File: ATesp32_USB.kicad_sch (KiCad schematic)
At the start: 17 parts, among them J1 USB_C_Receptacle_USB2.0_16P, U5 CP2102N-Axx-xQFN24

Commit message: update manf outputs
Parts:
- C15: Mouser 187-CL05B104KO5NNNC -> (none)
- U5: DigiKey (none) -> 336-5887-ND
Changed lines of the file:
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@@
 			)
 		)
-		(property "Mouser" "187-CL05B104KO5NNNC"
+		(property "Mouser" ""
 			(at 60.96 38.1 0)
 			(effects
@@
 			(at 85.09 73.66 0)
 			(effects
+				(font
+					(size 1.27 1.27)
+				)
+				(hide yes)
+			)
+		)
+		(property "DigiKey" "336-5887-ND"
+			(at 85.09 73.66 0)
+			(effects

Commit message: USB-UART Bridge LEDs had wrong orientation. Fixed
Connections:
- net GND: now also D5.1 (K), D6.1 (K); no longer D5.2 (A), D6.2 (A)
- net at R15.2: now also D6.2 (A); no longer D6.1 (K)
- net at R14.2: now also D5.2 (A); no longer D5.1 (K)
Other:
- moved on the sheet: D5, D6
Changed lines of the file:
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@@
 	(symbol
 		(lib_id "Device:LED_Small")
-		(at 105.41 92.71 270)
+		(at 105.41 92.71 90)
 		(unit 1)
 		(exclude_from_sim no)
@@
 		(fields_autoplaced yes)
 		(property "Reference" "D6"
-			(at 107.95 91.5034 90)
-			(effects
-				(font
-					(size 1.27 1.27)
-				)
-				(justify left)
+			(at 107.95 91.3764 90)
+			(effects
+				(font
+					(size 1.27 1.27)
+				)
+				(justify right)
 			)
 		)
 		(property "Value" "LED_Small"
-			(at 107.95 94.0434 90)
-			(effects
-				(font
-					(size 1.27 1.27)
-				)
-				(justify left)
+			(at 107.95 93.9164 90)
+			(effects
+				(font
+					(size 1.27 1.27)
+				)
+				(justify right)
 			)
 		)
@@
 	(symbol
 		(lib_id "Device:LED_Small")
-		(at 119.38 97.79 270)
+		(at 119.38 97.79 90)
 		(unit 1)
 		(exclude_from_sim no)
@@
 		(fields_autoplaced yes)
 		(property "Reference" "D5"
-			(at 121.92 96.5834 90)
-			(effects
-				(font
-					(size 1.27 1.27)
-				)
-				(justify left)
+			(at 121.92 96.4564 90)
+			(effects
+				(font
+					(size 1.27 1.27)
+				)
+				(justify right)
 			)
 		)
 		(property "Value" "LED_Small"
-			(at 121.92 99.1234 90)
-			(effects
-				(font
-					(size 1.27 1.27)
-				)
-				(justify left)
-			)
-		)
+			(at 121.92 98.9964 90)
+			(effects
+				(font
+					(size 1.27 1.27)
+				)
+				(justify right)
+			)
+		)

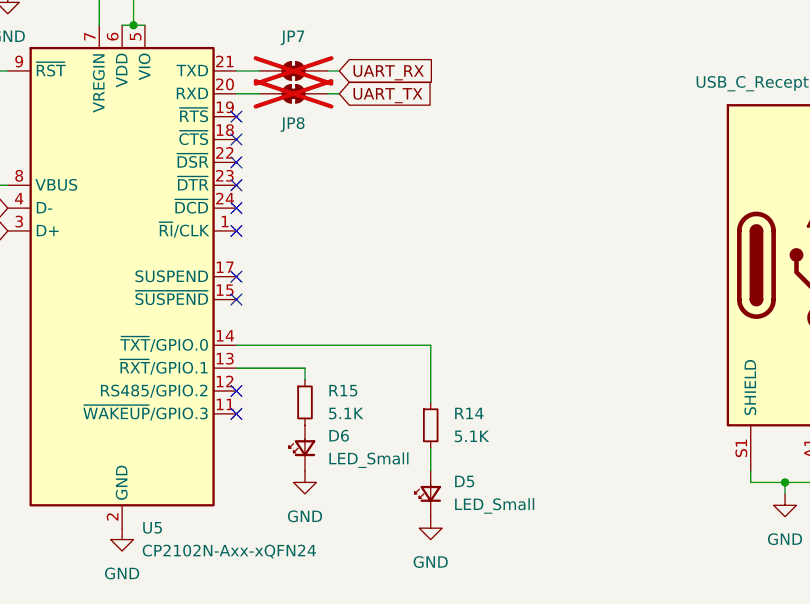
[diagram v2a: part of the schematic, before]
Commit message: LEDs were persistently on. Change to active low config see CP2102N datasheet fig 4.3
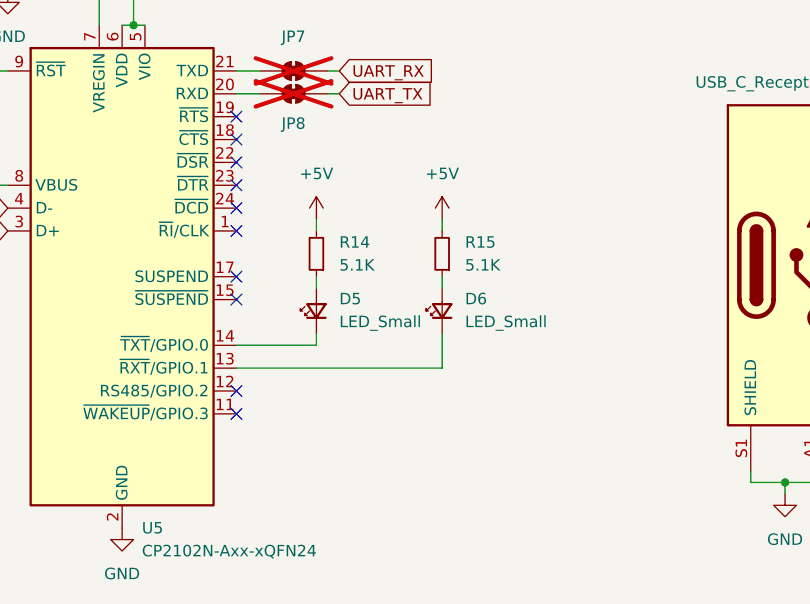
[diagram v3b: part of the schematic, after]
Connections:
- net +5V: now also R14.2, R15.2
- net GND: no longer D5.1 (K), D6.1 (K)
- net at D6.2 (A): now also R15.1; no longer R15.2
- net at D5.2 (A): now also R14.1; no longer R14.2
- net at U5.13 (~{RXT}/GPIO.1): now also D6.1 (K); no longer R15.1
- net at U5.14 (~{TXT}/GPIO.0): now also D5.1 (K); no longer R14.1
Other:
- moved on the sheet: D5, D6, R14, R15
